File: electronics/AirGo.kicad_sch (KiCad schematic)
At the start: 6 parts, among them J1 Power Connector, J2 FTDI Connector, J3 Motor Connector, J4 Button, U2 DRV8838, U3 ARDUINO_PRO_MINI

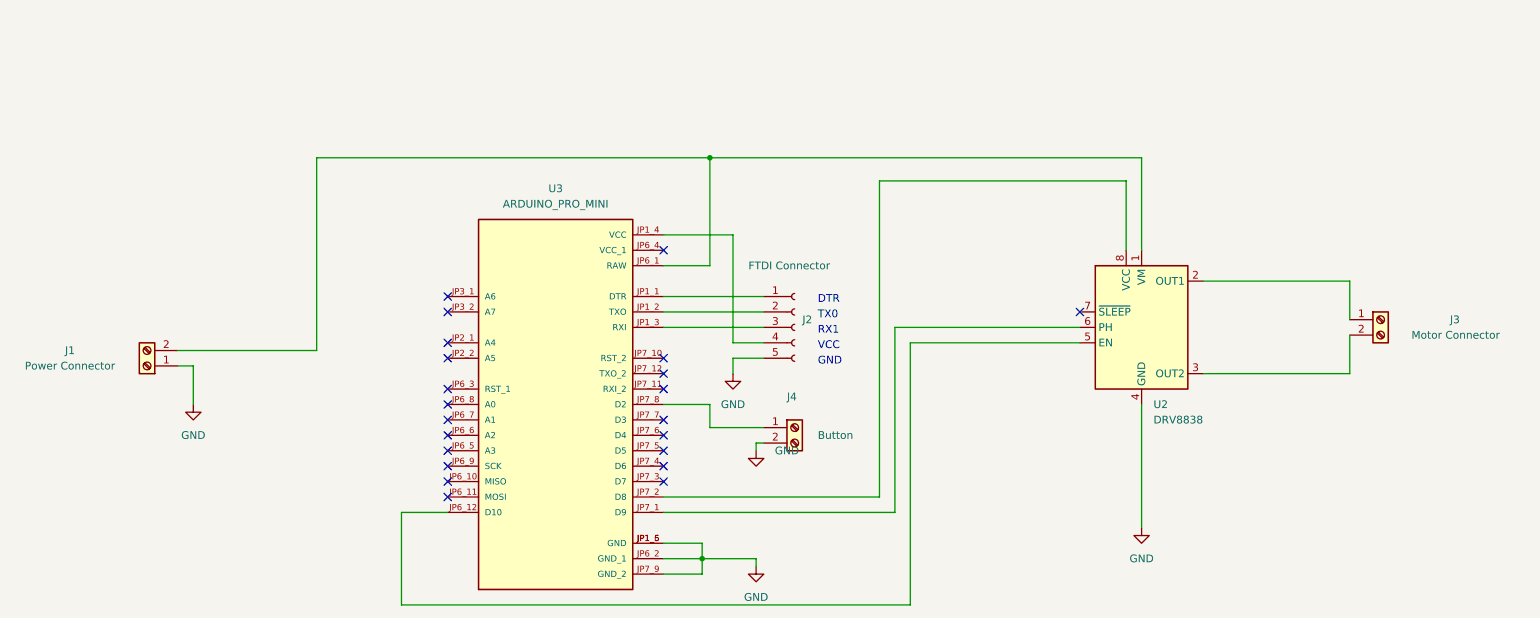
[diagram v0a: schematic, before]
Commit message: Fix pcb (edited with Kicad 8.0) and generate gerber & drill files
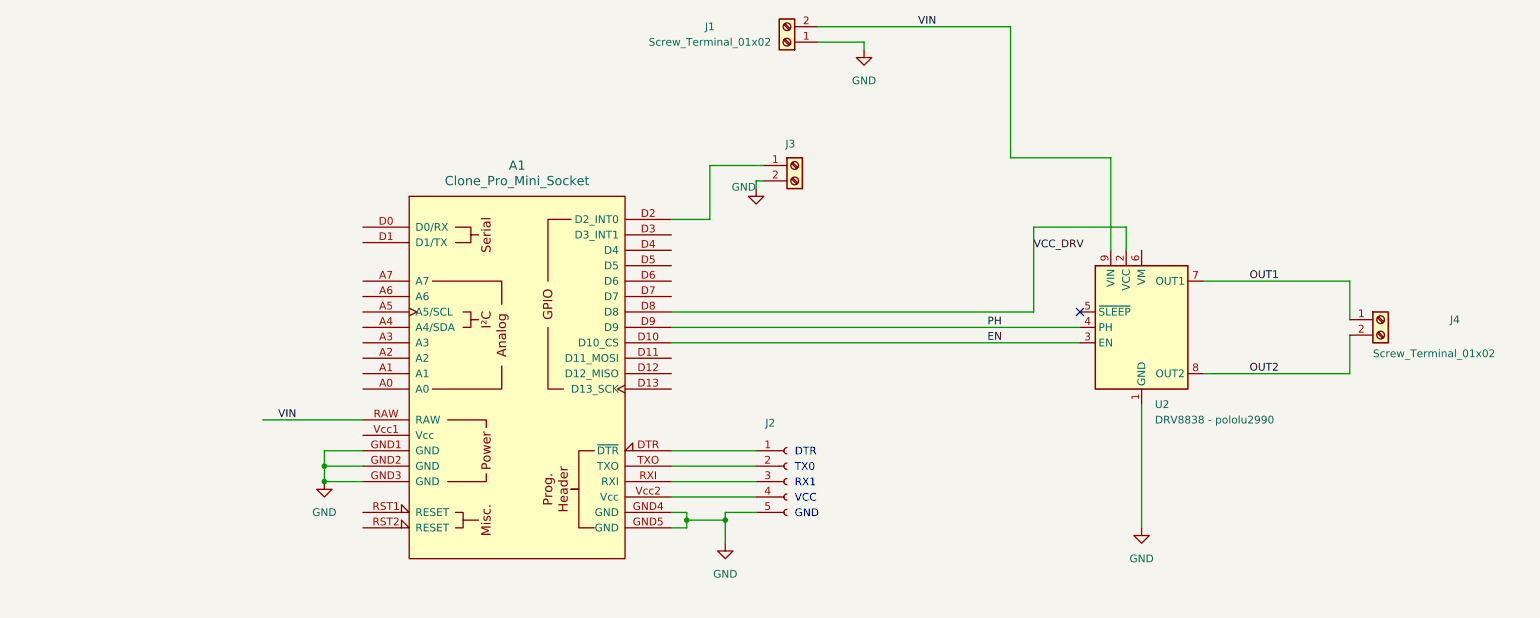
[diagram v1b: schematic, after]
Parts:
- removed U3: ARDUINO_PRO_MINI, MODULE_ARDUINO_PRO_MINI, symbol ARDUINO_PRO_MINI:ARDUINO_PRO_MINI
- added A1: Clone_Pro_Mini_Socket, PCM_arduino-library:Clone_Pro_Mini_Socket, symbol PCM_arduino-library:Clone_Pro_Mini_Socket
- J1: value Power Connector -> Screw_Terminal_01x02
- J2: value FTDI Connector -> Conn_01x05_Socket
- J3: renamed from J4; value Button -> Screw_Terminal_01x02
- J4: renamed from J3; value Motor Connector -> Screw_Terminal_01x02
- U2: value DRV8838 -> DRV8838 - pololu2990; footprint Package_DIP:DIP-10_W7.62mm_Socket -> Package_DIP:DIP-10_W7.62mm_LongPads; symbol Driver_Motor:DRV8838 -> pololu:DRV8838 - pololu2990
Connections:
- net GND: now also U2.1 (GND), U2.10 (GND), A1.GND1 (GND), A1.GND2 (GND), A1.GND3 (GND), A1.GND4 (GND), A1.GND5 (GND); no longer U2.4 (GND), U2.9 (GND)
- net at J3.1 (Pin_1): now also A1.D2 (D2_INT0)
- net VIN: now reaches J1.2 (Pin_2)
- net VIN: now also U2.9 (VIN), A1.RAW; no longer U2.1 (VM)
- net OUT1: now reaches J4.1 (Pin_1)
- net OUT1: now also U2.7 (OUT1); no longer U2.2 (OUT1)
- net EN: now reaches U2.3 (EN)
- net EN: now also A1.D10 (D10_CS); no longer J4.2 (Pin_2)
- net OUT2: now reaches U2.8 (OUT2)
- net OUT2: now also J4.2 (Pin_2)
- net at J2.1 (Pin_1): now also A1.DTR (~{DTR})
- net at J2.2 (Pin_2): now also A1.TXO
- net at J2.3 (Pin_3): now also A1.RXI
- net at J2.4 (Pin_4): now also A1.Vcc2 (Vcc)
- new net PH: A1.D9, U2.4 (PH)
- new net VCC_DRV: A1.D8, U2.2 (VCC)
- no-connect marks 22 -> 1
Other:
- moved on the sheet: J1, J2, J3
